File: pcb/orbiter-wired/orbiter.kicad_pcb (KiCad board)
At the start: 2 copper layers, 140 x 91 mm, 154 parts, among them J1 SWD, J2 AudioJack4, J3 I2C Extension, J4 AudioJack4, J5 Keyboard matrix, Q1 BSS138, Q2 BSS138, SW1 SW_SPDT, SW10 SW_Push, SW11 SW_Push, SW12 SW_Push, SW13 SW_Push, SW14 SW_Push, SW15 SW_Push, SW16 SW_Push, SW17 SW_Push, SW18 SW_Push, SW19 SW_Push, SW2 SW_Push, SW20 SW_Push, SW21 SW_Push, SW22 SW_Push, SW23 SW_Push, SW24 SW_Push, SW25 SW_Push, SW26 SW_Push, SW27 SW_Push, SW28 SW_SPDT, SW3 SW_Push, SW4 SW_Push, SW5 SW_Push, SW6 SW_Push, SW7 SW_Push, SW8 SW_Push, SW9 SW_Push, U1 TPS82140SILR

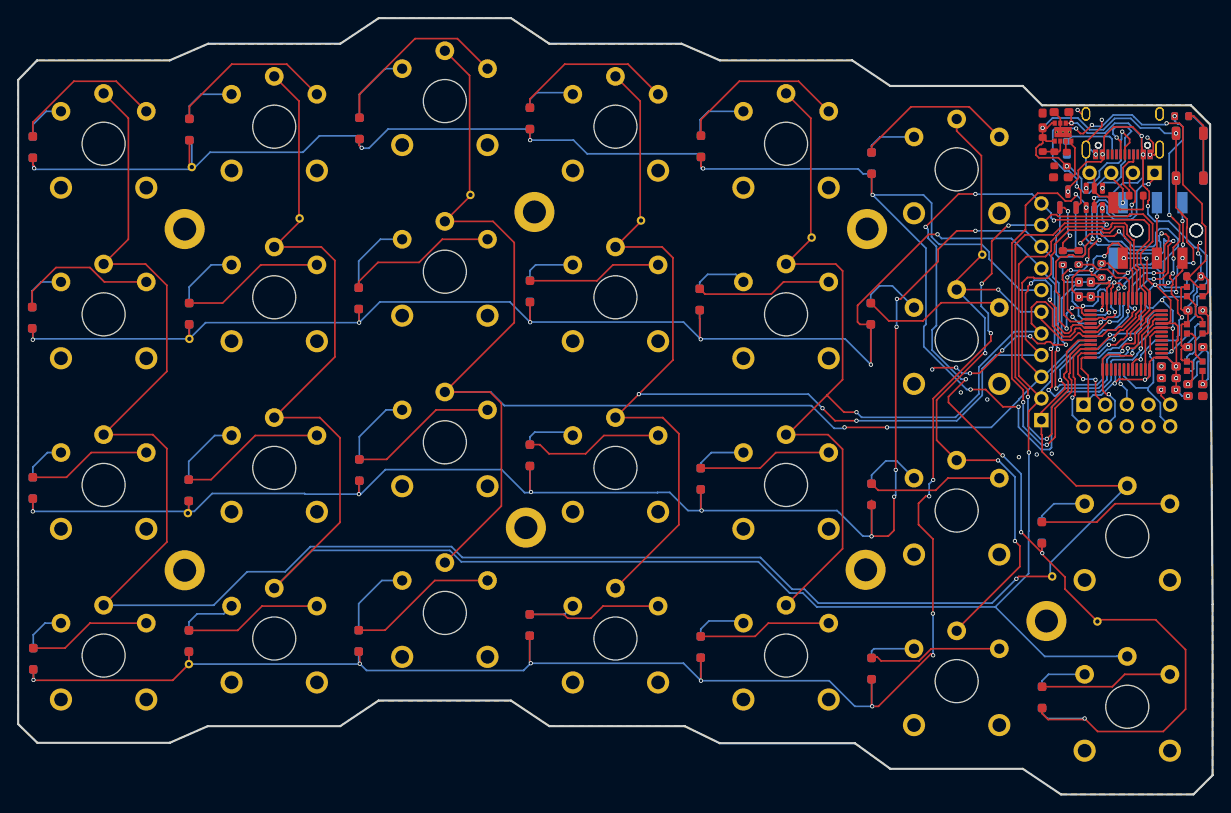
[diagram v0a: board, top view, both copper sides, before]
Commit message: Add pull-up for UART RX as well
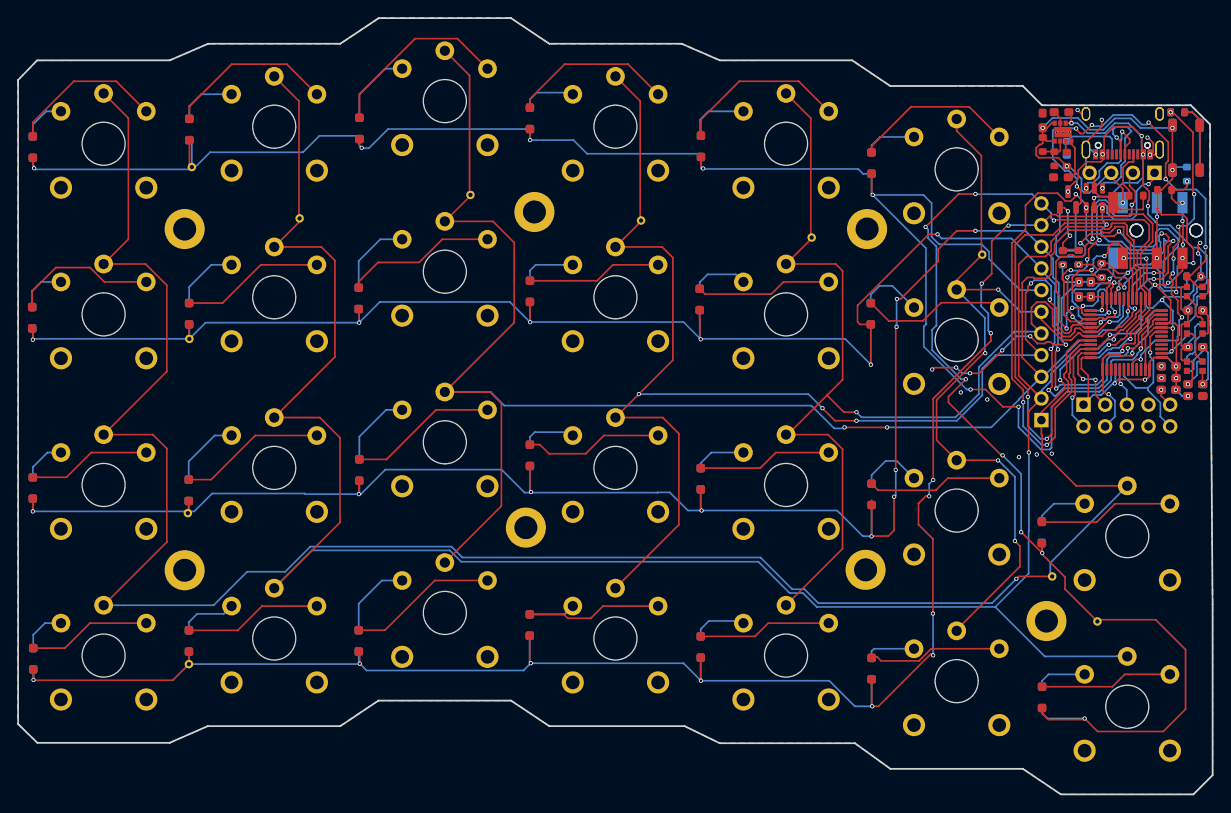
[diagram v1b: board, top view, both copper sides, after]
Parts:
- added R10: 8.2k, Resistor_SMD:R_0603_1608Metric, B.Cu at (223.2, 70.5)
- added R9: 8.2k, Resistor_SMD:R_0603_1608Metric, F.Cu at (220.6, 72.3)
- moved SW1 1.03 mm to (223.1, 67.3)
- moved SW28 1.03 mm to (223.1, 67.3)
- moved R6 0.66 mm to (222.2, 63.2)
- moved R7 0.66 mm to (222.2, 63.2)
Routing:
- net /TPS_VOUT: track 136.7 -> 142.0 mm
- net /USART_RX: track 33.8 -> 38.9 mm, vias 6 -> 8
- net /BOOT0: track 37.7 -> 39.0 mm, vias 6 -> 7
- net Net-(D59-DIN): track 50.4 -> 50.0 mm, vias 4 -> 6

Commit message: Add via stitching and graphics on front silk back
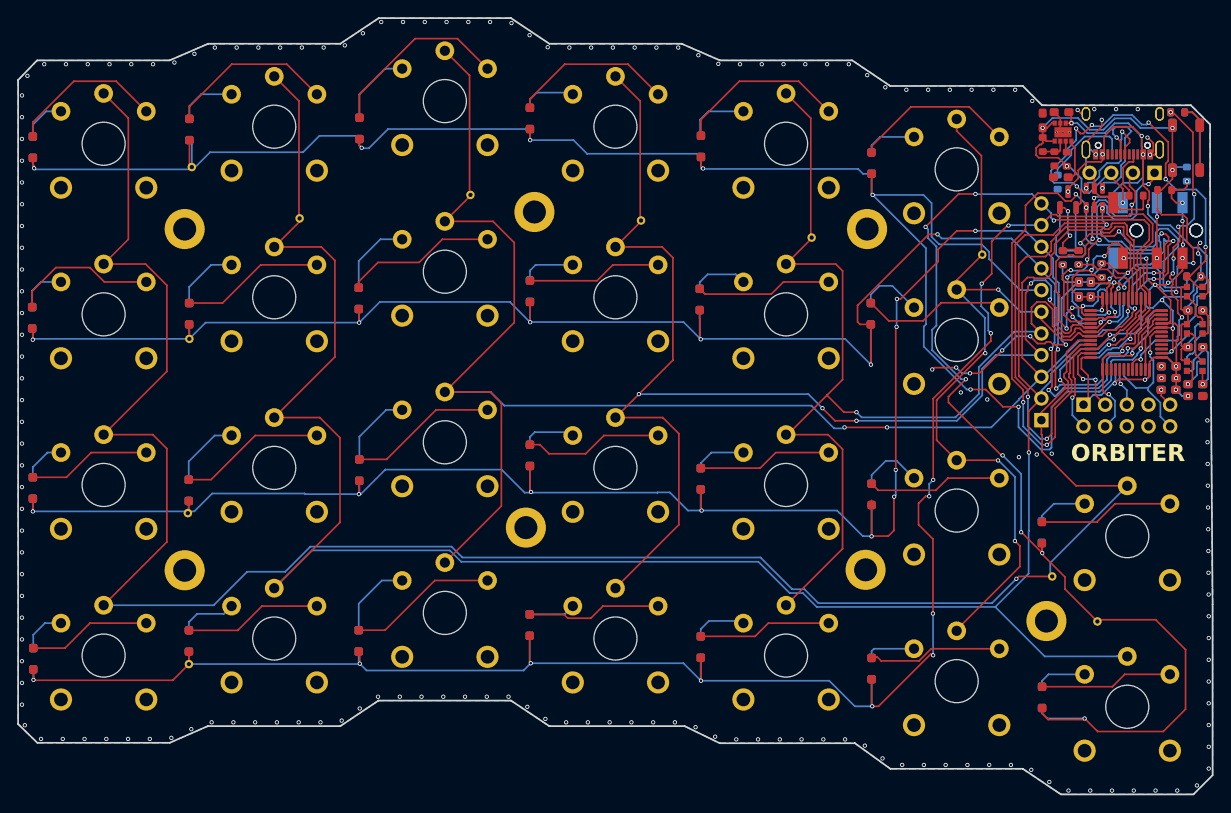
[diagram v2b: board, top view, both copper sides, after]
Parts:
- moved G*** 62.9 mm to (207.8, 65.9)
- moved R8 4.11 mm to (208.1, 71.4)
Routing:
- net Net-(USB_P2-CC): track 7.46 -> 11.0 mm
- net GND: vias 36 -> 191

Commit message: Edit project files to prepare for manufacturing
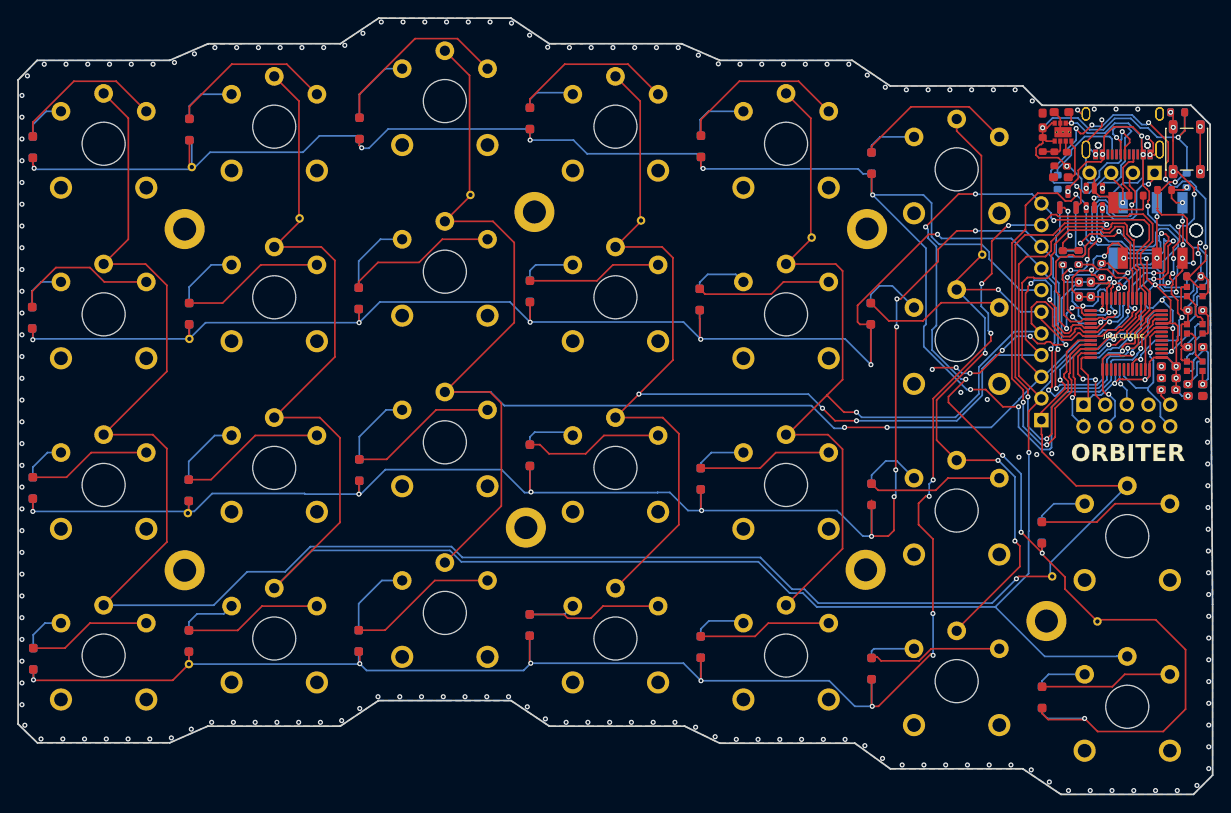
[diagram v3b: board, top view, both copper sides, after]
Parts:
- removed SW1, SW28: SW_SPDT, Button_Switch_SMD:SW_SPST_PTS647_Sx38
- added SW29: SW_Push, Button_Switch_SMD:SW_SPST_PTS647_Sx38, F.Cu at (223.2, 67.5)
- added SW30: SW_Push, Button_Switch_SMD:SW_SPST_PTS647_Sx38, B.Cu at (223.2, 67.5)
- moved R10 0.73 mm to (223.2, 71.2)
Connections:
- net /T_MCU_COL0 renamed /T_KEY_COL0
- net /T_MCU_COL1 renamed /T_KEY_COL1
- net /T_MCU_COL2 renamed /T_KEY_COL2
- net /T_MCU_COL3 renamed /T_KEY_COL3
- net /T_MCU_COL4 renamed /T_KEY_COL4
- net /T_MCU_COL5 renamed /T_KEY_COL5
- net /T_MCU_ROW0 renamed /T_KEY_ROW0
- net /T_MCU_ROW1 renamed /T_KEY_ROW1
- net /T_MCU_ROW2 renamed /T_KEY_ROW2
- net /T_MCU_ROW3 renamed /T_KEY_ROW3
- net /T_MCU_ROW4 renamed /T_KEY_ROW4
- R6 pad 1: Net-(SW1-B) -> /TPS_VOUT
- R7 pad 1: Net-(SW28-B) -> /TPS_VOUT
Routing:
- net Net-(SW1-B): track 8.04 -> 0.00 mm
- net Net-(SW28-B): track 8.02 -> 0.00 mm
- net /TPS_VOUT: track 142.0 -> 148.2 mm
- net GND: track 133.6 -> 139.0 mm, vias 191 -> 193
- net /BOOT0: track 39.0 -> 40.6 mm, vias 7 -> 9
- net Net-(D59-DIN): track 49.7 -> 50.5 mm
- net /USART_RX: track 38.9 -> 38.2 mm
